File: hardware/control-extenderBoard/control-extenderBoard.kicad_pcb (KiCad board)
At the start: 4 copper layers, 197.5 x 108.9 mm, 153 parts, among them J1 12V + GND (TP), J10 SCL6 + GND (TP), J11 SDA6 + GND (TP), J12 3V3 + GND (TP), J13 12V + GND (TP), J14 SCL6 + GND (TP), J15 SDA6 + GND (TP), J16 12V + GND (TP), J17 24V IN, J18 GND, J19 3V3 + GND (TP), J2 GND, J20 SCL6 + GND (TP), J21 SDA6 + GND (TP), J22 SDA, SCL - ESP32, J23 I2C Reserve SCL/GND, J24 I2C Reserve SCL/GND, J25 I2C Reserve SDA/GND, J26 I2C Reserve SDA/GND, J27 CAT6-Shield, J28 CAT6-Shield, J29 Chassis, J30 RX TX, J31 DIR, GND, J32 12V out, J33 5V out, J34 3V3 out, J4 3V3 + GND (TP), J5 GND, J6 SCL7 Differential (TP), J7 SDA7 Differential (TP), J8 RS485, P1 ISP, U1 MAX3485, U10 LM2576T-12, U13 AS5600_Breakout, U14 PCA9600D, U2 PCA9600D, U3 TCA9548A_1-to-8_I2C_Multiplex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, U4 LM2576T-3.3, U5 PCA9600D, U6 PCA82C251, U7 PCA82C251, U8 PCA9600D, U9 LM2576T-5

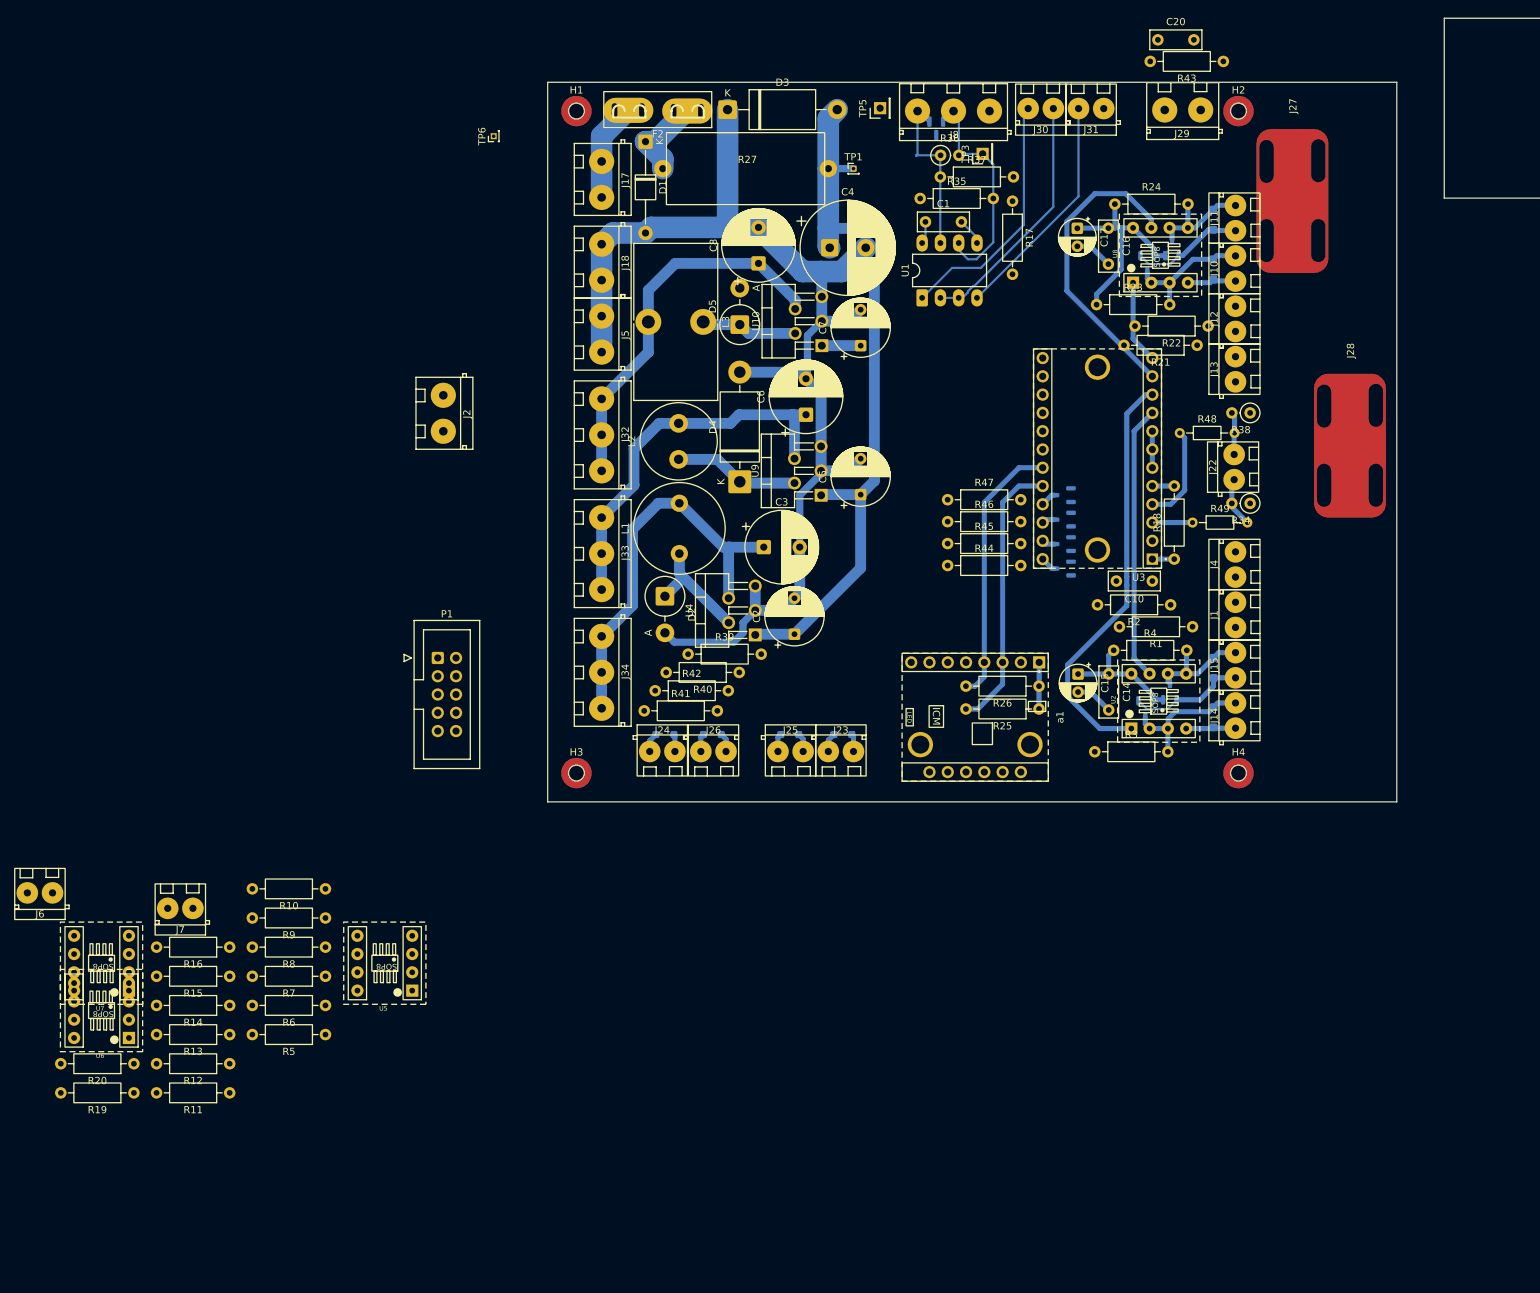
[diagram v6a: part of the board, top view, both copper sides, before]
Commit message: extenderBoard: Route RS485, I2C reserve, Add Testpoints, GND-Zones
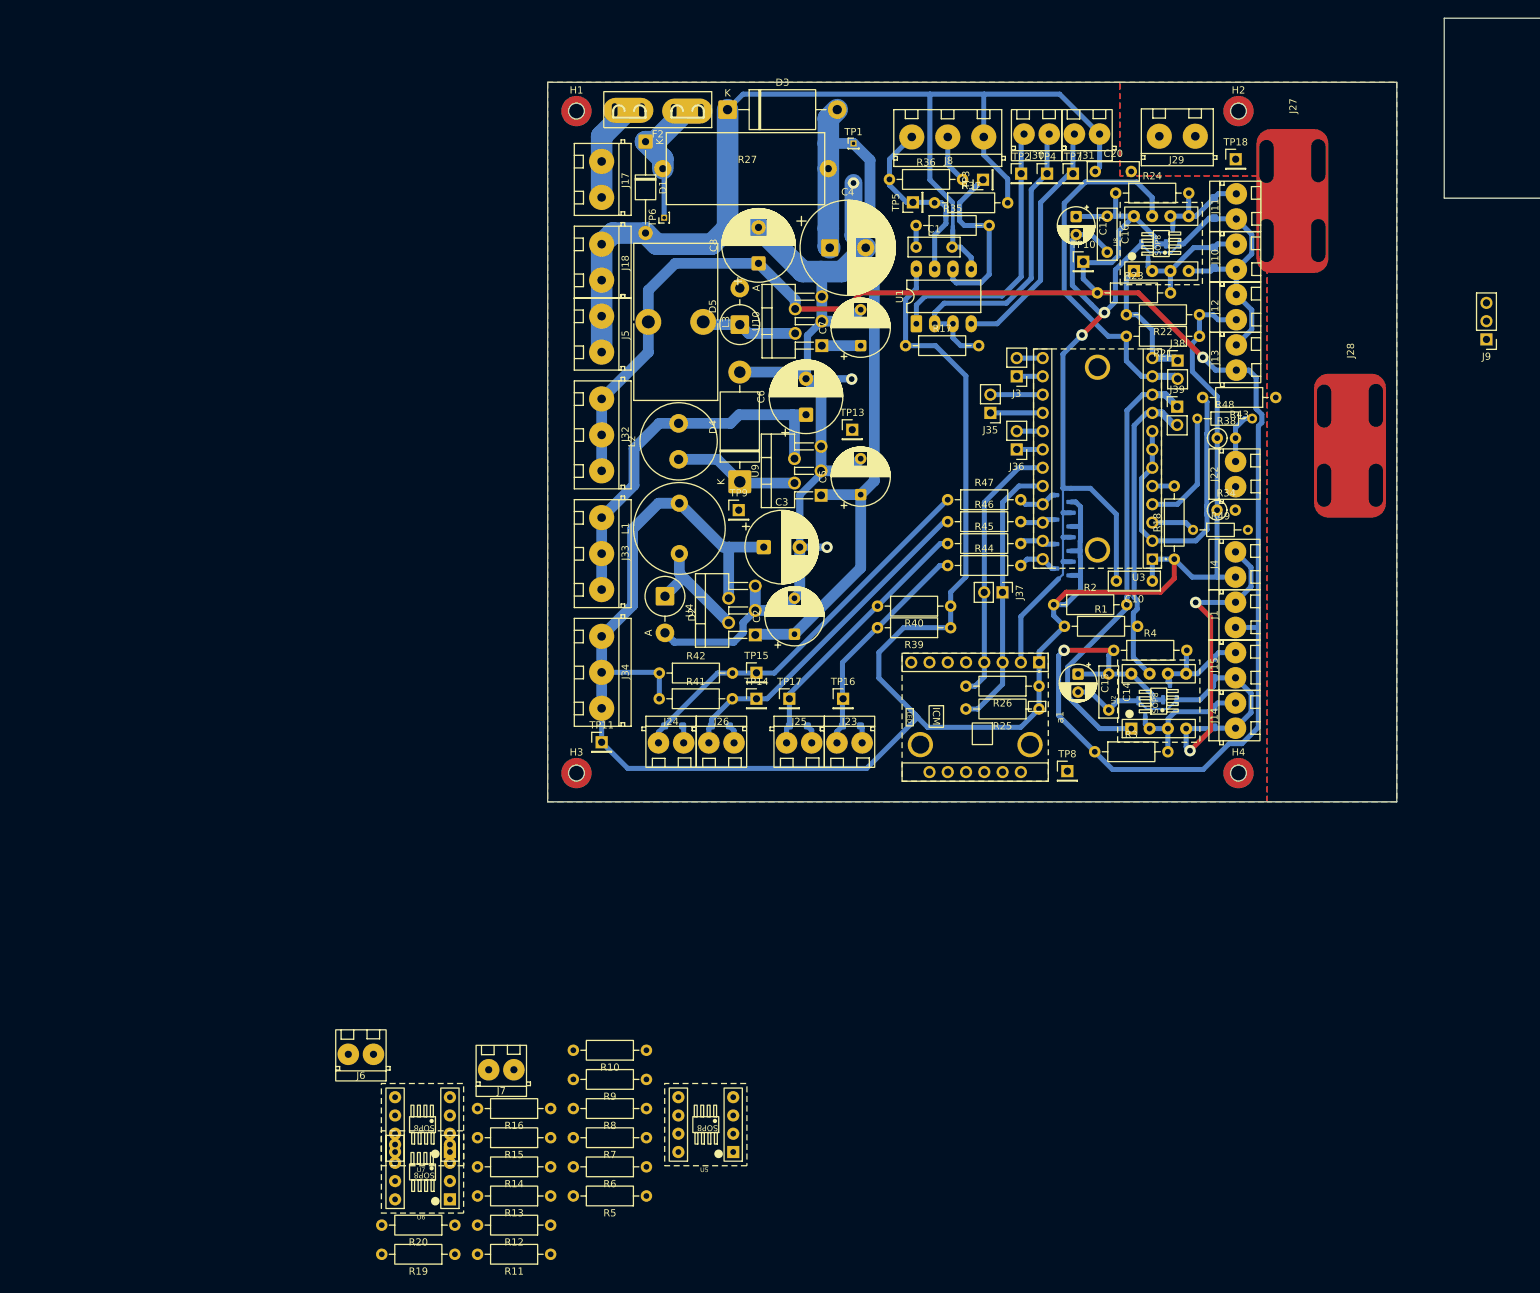
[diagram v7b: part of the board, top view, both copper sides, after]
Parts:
- removed J2: GND, terminals_libJonny:ScrewTerminal_P5mm_2Pin_FP10x8
- removed P1: ISP, Connector_IDC:IDC-Header_2x05_P2.54mm_Vertical
- added J3: Conn_01x02_Pin, Connector_PinHeader_2.54mm:PinHeader_1x02_P2.54mm_Vertical, F.Cu at (110.2, 70.9)
- added J35: Conn_01x02_Pin, Connector_PinHeader_2.54mm:PinHeader_1x02_P2.54mm_Vertical, F.Cu at (106.5, 75.9)
- added J36: Conn_01x02_Pin, Connector_PinHeader_2.54mm:PinHeader_1x02_P2.54mm_Vertical, F.Cu at (110.2, 81.0)
- added J37: Conn_01x02_Pin, Connector_PinHeader_2.54mm:PinHeader_1x02_P2.54mm_Vertical, F.Cu at (108.2, 100.9)
- added J38: Conn_01x02_Pin, Connector_PinHeader_2.54mm:PinHeader_1x02_P2.54mm_Vertical, F.Cu at (132.5, 68.7)
- added J39: Conn_01x02_Pin, Connector_PinHeader_2.54mm:PinHeader_1x02_P2.54mm_Vertical, F.Cu at (132.5, 75.1)
- added J9: Conn_01x03_Pin, Connector_PinHeader_2.54mm:PinHeader_1x03_P2.54mm_Vertical, F.Cu at (175.5, 65.7)
- added TP10: 12V, Connector_PinHeader_2.54mm:PinHeader_1x01_P2.54mm_Vertical, F.Cu at (119.4, 54.9)
- added TP11: 3V3, Connector_PinHeader_2.54mm:PinHeader_1x01_P2.54mm_Vertical, F.Cu at (52.5, 121.7)
- added TP13: GND, Connector_PinHeader_2.54mm:PinHeader_1x01_P2.54mm_Vertical, F.Cu at (87.3, 78.3)
- added TP14: SCL6, Connector_PinHeader_2.54mm:PinHeader_1x01_P2.54mm_Vertical, F.Cu at (74.0, 115.7)
- added TP15: SDA6, Connector_PinHeader_2.54mm:PinHeader_1x01_P2.54mm_Vertical, F.Cu at (74.0, 112.1)
- added TP16: SCL6, Connector_PinHeader_2.54mm:PinHeader_1x01_P2.54mm_Vertical, F.Cu at (86.1, 115.7)
- added TP17: SDA6, Connector_PinHeader_2.54mm:PinHeader_1x01_P2.54mm_Vertical, F.Cu at (78.6, 115.7)
- added TP18: Chassis, Connector_PinHeader_2.54mm:PinHeader_1x01_P2.54mm_Vertical, F.Cu at (140.6, 40.7)
- added TP2: RX, Connector_PinHeader_2.54mm:PinHeader_1x01_P2.54mm_Vertical, F.Cu at (110.8, 42.7)
- added TP4: DE, Connector_PinHeader_2.54mm:PinHeader_1x01_P2.54mm_Vertical, F.Cu at (114.4, 42.7)
- added TP7: TX, Connector_PinHeader_2.54mm:PinHeader_1x01_P2.54mm_Vertical, F.Cu at (118.0, 42.7)
- added TP8: GND, Connector_PinHeader_2.54mm:PinHeader_1x01_P2.54mm_Vertical, F.Cu at (117.2, 125.7)
- added TP9: 5V, Connector_PinHeader_2.54mm:PinHeader_1x01_P2.54mm_Vertical, F.Cu at (71.6, 89.5)
- J24: value I2C Reserve SCL/GND -> I2C Reserve SDA/GND
- J26: value I2C Reserve SDA/GND -> I2C Reserve SCL/GND
- R36: footprint Resistor_THT:R_Axial_DIN0207_L6.3mm_D2.5mm_P2.54mm_Vertical -> Resistor_THT:R_Axial_DIN0207_L6.3mm_D2.5mm_P10.16mm_Horizontal
- moved R6 49.9 mm to (58.7, 180.7)
- moved R8 49.9 mm to (58.7, 172.6)
- moved R9 49.9 mm to (58.7, 168.6)
- moved R10 49.9 mm to (58.7, 164.5)
- moved R11 49.9 mm to (45.4, 192.9)
- moved R12 49.9 mm to (45.4, 188.8)
- moved R14 49.9 mm to (45.4, 180.7)
- moved R16 49.9 mm to (45.4, 172.6)
- moved R19 49.9 mm to (32.1, 192.9)
- moved R20 49.9 mm to (32.1, 188.8)
- moved R5 49.9 mm to (58.7, 184.8)
- moved R7 49.9 mm to (58.7, 176.7)
- moved U5 49.9 mm to (67.0, 174.9)
- moved U6 49.9 mm to (27.6, 181.4)
- moved U7 49.9 mm to (27.6, 174.9)
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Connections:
- C18 pad 2: GND -> GND_REMOTE
- C19 pad 2: GND -> GND_REMOTE
- R41 pad 2: Net-(D17-A1) -> Net-(D20-A1)
- R42 pad 2: Net-(D20-A1) -> Net-(D17-A1)
- R46 pad 1: Net-(D17-A1) -> Net-(D20-A1)
- R47 pad 1: Net-(D20-A1) -> Net-(D17-A1)
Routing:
- net GND: track 244.5 -> 579.4 mm, vias 0 -> 7
- net +3V3: track 68.7 -> 341.5 mm
- net +12V: track 100.4 -> 277.1 mm, vias 0 -> 2
- net Net-(D17-A1): track 2.70 -> 55.1 mm
- net Net-(D20-A1): track 2.50 -> 47.6 mm
- net Net-(D6-A1): track 2.51 -> 37.6 mm
- net Net-(D18-A1): track 2.67 -> 31.7 mm
- net /RS485_DIR: track 34.7 -> 46.5 mm
- net /I2C1_SDA: track 42.4 -> 52.0 mm
- net /I2C3_SDA: track 0.00 -> 7.26 mm
- net /I2C3_SCL: track 0.00 -> 7.26 mm
- net /ESP32_SDA: track 6.99 -> 0.00 mm
- net /I2C1_SCL: track 11.6 -> 18.5 mm
- net Net-(D1-K): track 14.2 -> 21.1 mm
- net +24V filtered: track 108.1 -> 114.8 mm
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- added copper zone on B.Cu, net Chassis
- added copper zone on F.Cu, net Chassis
- added copper zone on B.Cu, net GND
- added copper zone on F.Cu, net GND
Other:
- board text added: "- Buck converters - 12V, 5V, 3V3 - I2C Multiplexer - 2x I2C 12V boosted - 2x I2C protected - 6-axis Gyroscope - RS485"
- board text added: "Armchair 31.08.2025 control-extenderBoard"
- board text added: "CHASSIS"
- board text removed: "Gate V2.0 31.12.2024 pcb_isolated-gate-control"
